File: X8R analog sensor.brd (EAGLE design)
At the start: 21.6 x 15.5 mm, 14 parts, among them IC1 MCP1703CB, U1 ATTINY13SOIC

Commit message: updated bypass caps as tantalums aren't needed
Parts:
- C2, C3: value 10uf 6.3V -> 1uf; device MyLib:CAP-0603 -> SparkFun-Capacitors:0603-CAP
- moved C2 4.49 mm to (5.08, 12.7), turned to 270 degrees
- moved C3 4.49 mm to (5.71, 8.26), turned to 180 degrees
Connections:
- net VCC: now also C3.1; no longer C2.1
- net VIN: now also C2.1; no longer C3.1
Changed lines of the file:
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@@
 </element>
 <element name="LED" library="SparkFun-LED" package="LED-0603" value="BLUE" x="6.985" y="12.7" smashed="yes">
-<attribute name="NAME" x="6.2865" y="11.176" size="0.4064" layer="25" rot="R90"/>
+<attribute name="NAME" x="6.4135" y="14.0335" size="0.4064" layer="25"/>
 <attribute name="VALUE" x="8.0645" y="11.684" size="0.4064" layer="27" rot="R90"/>
 </element>
@@
 <attribute name="NAME" x="7.5565" y="11.303" size="0.4064" layer="25" font="vector" rot="R180"/>
 <attribute name="VALUE" x="6.731" y="11.303" size="0.4064" layer="27" font="vector" rot="R180"/>
-</element>
-<element name="C2" library="MyLib" package="CAP-0603" value="10uf 6.3V" x="5.715" y="8.255" smashed="yes" rot="R180">
-<attribute name="NAME" x="7.239" y="9.398" size="0.4064" layer="25" font="vector" rot="R180"/>
-<attribute name="VALUE" x="6.731" y="9.398" size="0.4064" layer="27" font="vector" rot="R180"/>
-</element>
-<element name="C3" library="MyLib" package="CAP-0603" value="10uf 6.3V" x="5.08" y="12.7" smashed="yes" rot="R270">
-<attribute name="NAME" x="3.921" y="13.0175" size="0.4064" layer="25" rot="R270"/>
-<attribute name="VALUE" x="6.412" y="12.292" size="0.4064" layer="27" rot="R270"/>
 </element>
 <element name="FRAME1" library="SparkFun-Aesthetics" package="CREATIVE_COMMONS" value="FRAME-LETTER" x="-3.175" y="-11.43"/>
@@
 <attribute name="VALUE" x="19.5739" y="4.9155" size="0.8128" layer="21" ratio="15" rot="R270"/>
 </element>
+<element name="C2" library="SparkFun-Capacitors" package="0603-CAP" value="1uf" x="5.08" y="12.7" rot="R270"/>
+<element name="C3" library="SparkFun-Capacitors" package="0603-CAP" value="1uf" x="5.715" y="8.255" rot="R180"/>
 </elements>
 <signals>
 <signal name="GND">
-<contactref element="IC1" pad="1"/>
-<contactref element="C2" pad="2"/>
-<contactref element="C3" pad="2"/>
-<contactref element="C1" pad="2"/>
 <polygon width="0.4064" layer="1">
 <vertex x="0" y="15.5575"/>
@@
 <via x="19.05" y="3.4925" extent="1-16" drill="0.6"/>
 <via x="1.5875" y="1.5875" extent="1-16" drill="0.6"/>
+<contactref element="IC1" pad="1"/>
+<contactref element="C2" pad="2"/>
+<contactref element="C3" pad="2"/>
+<contactref element="C1" pad="2"/>
 </signal>
 <signal name="AIN">
@@
 <contactref element="IC1" pad="2"/>
 <contactref element="C1" pad="1"/>
-<contactref element="C2" pad="1"/>
-<wire x1="6.565" y1="8.255" x2="8.675" y2="8.255" width="0.4064" layer="1"/>
 <wire x1="10.475" y1="10.33" x2="10.475" y2="10.055" width="0.4064" layer="1"/>
 <wire x1="10.475" y1="10.055" x2="8.675" y2="8.255" width="0.4064" layer="1"/>
@@
 <wire x1="4.865" y1="9.74" x2="5.3975" y2="9.2075" width="0.4064" layer="1"/>
 <wire x1="5.3975" y1="9.2075" x2="5.6125" y2="9.2075" width="0.4064" layer="1"/>
-<wire x1="5.6125" y1="9.2075" x2="6.565" y2="8.255" width="0.4064" layer="1"/>
 <wire x1="4.1275" y1="4.445" x2="4.1275" y2="5.715" width="0.4064" layer="1"/>
 <wire x1="4.1275" y1="5.715" x2="5.08" y2="6.6675" width="0.4064" layer="1"/>
 <wire x1="5.08" y1="6.6675" x2="5.715" y2="6.6675" width="0.4064" layer="1"/>
 <wire x1="5.715" y1="6.6675" x2="6.565" y2="7.5175" width="0.4064" layer="1"/>
-<wire x1="6.565" y1="7.5175" x2="6.565" y2="8.255" width="0.4064" layer="1"/>
+<contactref element="C3" pad="1"/>
+<wire x1="5.6125" y1="9.2075" x2="6.565" y2="8.255" width="0.4064" layer="1"/>
+<wire x1="6.565" y1="8.255" x2="6.565" y2="7.5175" width="0.4064" layer="1"/>
+<wire x1="6.565" y1="8.255" x2="6.35" y2="8.255" width="0.4064" layer="1"/>
+<wire x1="6.565" y1="8.255" x2="8.675" y2="8.255" width="0.4064" layer="1"/>
 </signal>
 <signal name="N$7">
@@
 <contactref element="S-PORT" pad="2"/>
 <contactref element="IC1" pad="3"/>
-<contactref element="C3" pad="1"/>
-<wire x1="2.6425" y1="11.1125" x2="5.08" y2="13.55" width="0.4064" layer="1"/>
 <wire x1="9.525" y1="12.53" x2="9.525" y2="14.2875" width="0.4064" layer="1"/>
 <wire x1="9.525" y1="14.2875" x2="9.2075" y2="14.605" width="0.4064" layer="1"/>
 <wire x1="9.2075" y1="14.605" x2="6.135" y2="14.605" width="0.4064" layer="1"/>
+<wire x1="2.6425" y1="11.1125" x2="1.905" y2="11.1125" width="0.4064" layer="1"/>
+<contactref element="C2" pad="1"/>
 <wire x1="6.135" y1="14.605" x2="5.08" y2="13.55" width="0.4064" layer="1"/>
-<wire x1="2.6425" y1="11.1125" x2="1.905" y2="11.1125" width="0.4064" layer="1"/>
+<wire x1="5.08" y1="13.55" x2="2.6425" y2="11.1125" width="0.4064" layer="1"/>
 </signal>
 <signal name="AIN-O">

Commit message: updated for a bypass cap on the AIN side, and changed the 3 pin connector for AIN to a 2 pin
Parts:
- removed ANALOGIN: (no value), SparkFun-Connectors:1X03
- added ANALOG-IN: M02PTH, SparkFun-Connectors:1X02
- added C4: .1uf, SparkFun-Capacitors:0603-CAP
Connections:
- net AIN: now also ANALOG-IN.1; no longer ANALOGIN.1
- net AIN-O: now also C4.1
- net GND: now also ANALOG-IN.2, C4.2; no longer ANALOGIN.3
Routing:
- net AIN: track 3.24 -> 5.78 mm
- net AIN-O: track 19.9 -> 18.7 mm
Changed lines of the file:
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@@
 </autorouter>
 <elements>
-<element name="C1" library="SparkFun-Capacitors" package="0603-CAP" value=".1uf" x="9.525" y="8.255" smashed="yes">
-<attribute name="NAME" x="11.049" y="9.398" size="0.4064" layer="25" font="vector" rot="R180"/>
-<attribute name="VALUE" x="8.509" y="7.112" size="0.4064" layer="27" font="vector"/>
-</element>
-<element name="U1" library="SparkFun-DigitalIC" package="SO08" value="ATTINY13SOIC" x="14.605" y="7.9375" smashed="yes" rot="R180">
-<attribute name="VALUE" x="15.875" y="8.5725" size="0.4064" layer="27" rot="R180"/>
-<attribute name="NAME" x="11.43" y="6.985" size="0.4064" layer="25"/>
-</element>
+<element name="C1" library="SparkFun-Capacitors" package="0603-CAP" value=".1uf" x="9.525" y="8.255"/>
+<element name="U1" library="SparkFun-DigitalIC" package="SO08" value="ATTINY13SOIC" x="14.605" y="7.9375" rot="R180"/>
 <element name="IC1" library="linear" package="SOT23" value="MCP1703CB" x="9.525" y="11.43" smashed="yes">
 <attribute name="NAME" x="7.9375" y="12.3825" size="0.4064" layer="25"/>
@@
 <attribute name="NAME" x="2.9337" y="6.9088" size="0.4064" layer="25" ratio="10" rot="R180"/>
 <attribute name="VALUE" x="5.08" y="7.3025" size="1.27" layer="27" rot="R90"/>
-</element>
-<element name="ANALOGIN" library="SparkFun-Connectors" package="1X03" value="" x="19.685" y="8.5725" smashed="yes" rot="R90">
-<attribute name="NAME" x="18.1737" y="7.3787" size="0.4064" layer="25" ratio="10" rot="R90"/>
-<attribute name="VALUE" x="22.86" y="7.3025" size="1.27" layer="27" rot="R90"/>
 </element>
 <element name="LED" library="SparkFun-LED" package="LED-0603" value="BLUE" x="6.985" y="12.7" smashed="yes">
@@
 <element name="C2" library="SparkFun-Capacitors" package="0603-CAP" value="1uf" x="5.08" y="12.7" rot="R270"/>
 <element name="C3" library="SparkFun-Capacitors" package="0603-CAP" value="1uf" x="5.715" y="8.255" rot="R180"/>
+<element name="C4" library="SparkFun-Capacitors" package="0603-CAP" value=".1uf" x="15.5575" y="1.905" rot="R180"/>
+<element name="ANALOG-IN" library="SparkFun-Connectors" package="1X02" value="M02PTH" x="19.685" y="11.1125" smashed="yes" rot="R90">
+<attribute name="NAME" x="18.0213" y="9.1313" size="0.4064" layer="25" ratio="10"/>
+<attribute name="VALUE" x="22.86" y="9.8425" size="1.27" layer="27" rot="R90"/>
+</element>
 </elements>
 <signals>
@@
 </polygon>
 <contactref element="S-PORT" pad="1"/>
-<contactref element="ANALOGIN" pad="3"/>
 <contactref element="LED" pad="C"/>
 <contactref element="U1" pad="4"/>
@@
 <contactref element="R3" pad="1"/>
 <via x="10.795" y="13.97" extent="1-16" drill="0.6"/>
-<via x="13.97" y="2.2225" extent="1-16" drill="0.6"/>
+<via x="12.7" y="1.905" extent="1-16" drill="0.6"/>
 <via x="11.43" y="4.7625" extent="1-16" drill="0.6"/>
 <via x="19.05" y="3.4925" extent="1-16" drill="0.6"/>
@@
 <contactref element="C3" pad="2"/>
 <contactref element="C1" pad="2"/>
+<contactref element="C4" pad="2"/>
+<contactref element="ANALOG-IN" pad="2"/>
+<via x="19.685" y="7.9375" extent="1-16" drill="0.6"/>
 </signal>
 <signal name="AIN">
-<contactref element="ANALOGIN" pad="1"/>
 <contactref element="R2" pad="2"/>
-<wire x1="19.685" y1="8.5725" x2="18.0975" y2="6.985" width="0.4064" layer="1"/>
-<wire x1="18.0975" y1="6.985" x2="18.0975" y2="5.9925" width="0.4064" layer="1"/>
+<contactref element="ANALOG-IN" pad="1"/>
+<wire x1="19.685" y1="11.1125" x2="18.0975" y2="9.525" width="0.4064" layer="1"/>
+<wire x1="18.0975" y1="9.525" x2="18.0975" y2="5.9925" width="0.4064" layer="1"/>
 </signal>
 <signal name="VCC">
@@
 <contactref element="S-PORT" pad="2"/>
 <contactref element="IC1" pad="3"/>
-<wire x1="9.525" y1="12.53" x2="9.525" y2="14.2875" width="0.4064" layer="1"/>
-<wire x1="9.525" y1="14.2875" x2="9.2075" y2="14.605" width="0.4064" layer="1"/>
-<wire x1="9.2075" y1="14.605" x2="6.135" y2="14.605" width="0.4064" layer="1"/>
 <wire x1="2.6425" y1="11.1125" x2="1.905" y2="11.1125" width="0.4064" layer="1"/>
 <contactref element="C2" pad="1"/>
 <wire x1="6.135" y1="14.605" x2="5.08" y2="13.55" width="0.4064" layer="1"/>
 <wire x1="5.08" y1="13.55" x2="2.6425" y2="11.1125" width="0.4064" layer="1"/>
+<wire x1="9.525" y1="12.53" x2="9.525" y2="13.97" width="0.4064" layer="1"/>
+<wire x1="9.525" y1="13.97" x2="8.89" y2="14.605" width="0.4064" layer="1"/>
+<wire x1="8.89" y1="14.605" x2="6.135" y2="14.605" width="0.4064" layer="1"/>
 </signal>
 <signal name="AIN-O">
@@
 <contactref element="R3" pad="2"/>
 <contactref element="R2" pad="1"/>
+<contactref element="C4" pad="1"/>
+<wire x1="6.6675" y1="1.905" x2="7.9375" y2="0.635" width="0.4064" layer="1"/>
+<wire x1="7.9375" y1="0.635" x2="15.24" y2="0.635" width="0.4064" layer="1"/>
 <wire x1="20.0025" y1="0.9925" x2="18.0975" y2="0.9925" width="0.4064" layer="1"/>
-<wire x1="18.0975" y1="0.9925" x2="17.4225" y2="0.9925" width="0.4064" layer="1"/>
-<wire x1="17.4225" y1="0.9925" x2="15.24" y2="3.175" width="0.4064" layer="1"/>
-<wire x1="15.24" y1="3.175" x2="15.24" y2="5.3213" width="0.4064" layer="1"/>
-<wire x1="6.6675" y1="1.905" x2="7.9375" y2="0.635" width="0.4064" layer="1"/>
-<wire x1="7.9375" y1="0.635" x2="17.74" y2="0.635" width="0.4064" layer="1"/>
-<wire x1="17.74" y1="0.635" x2="18.0975" y2="0.9925" width="0.4064" layer="1"/>
+<wire x1="18.0975" y1="0.9925" x2="17.185" y2="1.905" width="0.4064" layer="1"/>
+<wire x1="17.185" y1="1.905" x2="16.4075" y2="1.905" width="0.4064" layer="1"/>
+<wire x1="16.4075" y1="1.905" x2="15.24" y2="3.0725" width="0.4064" layer="1"/>
+<wire x1="15.24" y1="3.0725" x2="15.24" y2="5.3213" width="0.4064" layer="1"/>
+<wire x1="16.4075" y1="1.905" x2="16.4075" y2="1.8025" width="0.4064" layer="1"/>
+<wire x1="16.4075" y1="1.8025" x2="15.24" y2="0.635" width="0.4064" layer="1"/>
 </signal>
 </signals>

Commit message: reverted back to the 3 pin connector on AIN
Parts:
- ANALOG-IN: value M02PTH -> (none); device SparkFun-Connectors:1X02 -> SparkFun-Connectors:1X03
- moved ANALOG-IN 2.54 mm to (19.7, 8.57)
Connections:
- net GND: now also ANALOG-IN.3; no longer ANALOG-IN.2
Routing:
- net AIN: track 5.78 -> 3.24 mm
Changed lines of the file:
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@@
 <element name="C3" library="SparkFun-Capacitors" package="0603-CAP" value="1uf" x="5.715" y="8.255" rot="R180"/>
 <element name="C4" library="SparkFun-Capacitors" package="0603-CAP" value=".1uf" x="15.5575" y="1.905" rot="R180"/>
-<element name="ANALOG-IN" library="SparkFun-Connectors" package="1X02" value="M02PTH" x="19.685" y="11.1125" smashed="yes" rot="R90">
-<attribute name="NAME" x="18.0213" y="9.1313" size="0.4064" layer="25" ratio="10"/>
-<attribute name="VALUE" x="22.86" y="9.8425" size="1.27" layer="27" rot="R90"/>
+<element name="ANALOG-IN" library="SparkFun-Connectors" package="1X03" value="" x="19.685" y="8.5725" smashed="yes" rot="R90">
+<attribute name="NAME" x="18.1737" y="7.2263" size="0.4064" layer="25" ratio="10" rot="R90"/>
+<attribute name="VALUE" x="22.86" y="7.3025" size="1.27" layer="27" rot="R90"/>
 </element>
 </elements>
@@
 <contactref element="C1" pad="2"/>
 <contactref element="C4" pad="2"/>
-<contactref element="ANALOG-IN" pad="2"/>
-<via x="19.685" y="7.9375" extent="1-16" drill="0.6"/>
+<contactref element="ANALOG-IN" pad="3"/>
 </signal>
 <signal name="AIN">
 <contactref element="R2" pad="2"/>
 <contactref element="ANALOG-IN" pad="1"/>
-<wire x1="19.685" y1="11.1125" x2="18.0975" y2="9.525" width="0.4064" layer="1"/>
-<wire x1="18.0975" y1="9.525" x2="18.0975" y2="5.9925" width="0.4064" layer="1"/>
+<wire x1="18.0975" y1="5.9925" x2="18.0975" y2="6.985" width="0.4064" layer="1"/>
+<wire x1="18.0975" y1="6.985" x2="19.685" y2="8.5725" width="0.4064" layer="1"/>
 </signal>
 <signal name="VCC">

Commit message: small non-functional tweaks to the board layout, updated gerbers
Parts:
- moved C4 1.00 mm to (16.5, 2.22), turned to 90 degrees
- moved R2 0.32 mm to (18.4, 3.49)
- moved R3 0.32 mm to (20.3, 3.49)
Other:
- board text added: "20131024-1"
- board text removed: "20131022-1"
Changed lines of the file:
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@@
 <text x="3.4925" y="8.255" size="0.8128" layer="21">-</text>
 <text x="17.78" y="8.255" size="0.8128" layer="22" font="vector" rot="MR0">X8R S.port-2-analog</text>
-<text x="17.78" y="6.985" size="0.6096" layer="22" font="vector" rot="MR0">20131022-1</text>
+<text x="17.78" y="6.985" size="0.6096" layer="22" font="vector" rot="MR0">20131024-1</text>
 <dimension x1="0" y1="0" x2="0" y2="15.5575" x3="-2.54" y3="7.77875" textsize="1.778" layer="49"/>
 <dimension x1="0" y1="15.5575" x2="21.59" y2="15.5575" x3="10.795" y3="17.78" textsize="1.778" layer="49"/>
@@
 <attribute name="VALUE" x="11.43" y="10.4775" size="1.27" layer="27"/>
 </element>
-<element name="R2" library="SparkFun-Passives" package="1/6W-RES" value="" x="18.0975" y="3.4925" smashed="yes" rot="R90">
-<attribute name="NAME" x="17.4652" y="4.7587" size="0.6096" layer="25" rot="R270"/>
-<attribute name="VALUE" x="18.5261" y="2.0695" size="0.8128" layer="21" ratio="15" rot="R90"/>
-</element>
-<element name="R3" library="SparkFun-Passives" package="1/6W-RES" value="" x="20.0025" y="3.4925" smashed="yes" rot="R270">
-<attribute name="NAME" x="19.3702" y="4.7587" size="0.6096" layer="25" rot="R270"/>
-<attribute name="VALUE" x="19.5739" y="4.9155" size="0.8128" layer="21" ratio="15" rot="R270"/>
+<element name="R2" library="SparkFun-Passives" package="1/6W-RES" value="" x="18.415" y="3.4925" smashed="yes" rot="R90">
+<attribute name="NAME" x="17.7827" y="4.7587" size="0.6096" layer="25" rot="R270"/>
+<attribute name="VALUE" x="18.8436" y="2.0695" size="0.8128" layer="21" ratio="15" rot="R90"/>
+</element>
+<element name="R3" library="SparkFun-Passives" package="1/6W-RES" value="" x="20.32" y="3.4925" smashed="yes" rot="R270">
+<attribute name="NAME" x="19.6877" y="4.7587" size="0.6096" layer="25" rot="R270"/>
+<attribute name="VALUE" x="19.8914" y="4.9155" size="0.8128" layer="21" ratio="15" rot="R270"/>
 </element>
 <element name="C2" library="SparkFun-Capacitors" package="0603-CAP" value="1uf" x="5.08" y="12.7" rot="R270"/>
 <element name="C3" library="SparkFun-Capacitors" package="0603-CAP" value="1uf" x="5.715" y="8.255" rot="R180"/>
-<element name="C4" library="SparkFun-Capacitors" package="0603-CAP" value=".1uf" x="15.5575" y="1.905" rot="R180"/>
+<element name="C4" library="SparkFun-Capacitors" package="0603-CAP" value=".1uf" x="16.51" y="2.2225" rot="R90"/>
 <element name="ANALOG-IN" library="SparkFun-Connectors" package="1X03" value="" x="19.685" y="8.5725" smashed="yes" rot="R90">
 <attribute name="NAME" x="18.1737" y="7.2263" size="0.4064" layer="25" ratio="10" rot="R90"/>
@@
 <signals>
 <signal name="GND">
-<polygon width="0.4064" layer="1">
+<polygon width="0.4064" layer="1" orphans="yes">
 <vertex x="0" y="15.5575"/>
 <vertex x="21.59" y="15.5575"/>
@@
 <vertex x="0" y="0"/>
 </polygon>
-<polygon width="0.4064" layer="16">
+<polygon width="0.4064" layer="16" orphans="yes">
 <vertex x="0" y="15.5575"/>
 <vertex x="21.59" y="15.5575"/>
@@
 <contactref element="U1" pad="4"/>
 <contactref element="ISP" pad="6"/>
-<via x="3.81" y="14.605" extent="1-16" drill="0.6"/>
 <contactref element="R3" pad="1"/>
-<via x="10.795" y="13.97" extent="1-16" drill="0.6"/>
-<via x="12.7" y="1.905" extent="1-16" drill="0.6"/>
-<via x="11.43" y="4.7625" extent="1-16" drill="0.6"/>
-<via x="19.05" y="3.4925" extent="1-16" drill="0.6"/>
-<via x="1.5875" y="1.5875" extent="1-16" drill="0.6"/>
+<via x="10.795" y="13.97" extent="1-16" drill="0.5"/>
+<via x="19.3675" y="3.4925" extent="1-16" drill="0.5"/>
+<via x="1.5875" y="1.5875" extent="1-16" drill="0.5"/>
 <contactref element="IC1" pad="1"/>
 <contactref element="C2" pad="2"/>
@@
 <contactref element="C4" pad="2"/>
 <contactref element="ANALOG-IN" pad="3"/>
+<via x="11.43" y="6.985" extent="1-16" drill="0.5"/>
 </signal>
 <signal name="AIN">
 <contactref element="R2" pad="2"/>
 <contactref element="ANALOG-IN" pad="1"/>
-<wire x1="18.0975" y1="5.9925" x2="18.0975" y2="6.985" width="0.4064" layer="1"/>
-<wire x1="18.0975" y1="6.985" x2="19.685" y2="8.5725" width="0.4064" layer="1"/>
+<wire x1="19.685" y1="8.5725" x2="18.415" y2="7.3025" width="0.4064" layer="1"/>
+<wire x1="18.415" y1="7.3025" x2="18.415" y2="5.9925" width="0.4064" layer="1"/>
 </signal>
 <signal name="VCC">
@@
 <contactref element="C4" pad="1"/>
 <wire x1="6.6675" y1="1.905" x2="7.9375" y2="0.635" width="0.4064" layer="1"/>
-<wire x1="7.9375" y1="0.635" x2="15.24" y2="0.635" width="0.4064" layer="1"/>
-<wire x1="20.0025" y1="0.9925" x2="18.0975" y2="0.9925" width="0.4064" layer="1"/>
-<wire x1="18.0975" y1="0.9925" x2="17.185" y2="1.905" width="0.4064" layer="1"/>
-<wire x1="17.185" y1="1.905" x2="16.4075" y2="1.905" width="0.4064" layer="1"/>
-<wire x1="16.4075" y1="1.905" x2="15.24" y2="3.0725" width="0.4064" layer="1"/>
-<wire x1="15.24" y1="3.0725" x2="15.24" y2="5.3213" width="0.4064" layer="1"/>
-<wire x1="16.4075" y1="1.905" x2="16.4075" y2="1.8025" width="0.4064" layer="1"/>
-<wire x1="16.4075" y1="1.8025" x2="15.24" y2="0.635" width="0.4064" layer="1"/>
+<wire x1="7.9375" y1="0.635" x2="15.7725" y2="0.635" width="0.4064" layer="1"/>
+<wire x1="20.32" y1="0.9925" x2="18.415" y2="0.9925" width="0.4064" layer="1"/>
+<wire x1="18.415" y1="0.9925" x2="16.89" y2="0.9925" width="0.4064" layer="1"/>
+<wire x1="16.89" y1="0.9925" x2="16.51" y2="1.3725" width="0.4064" layer="1"/>
+<wire x1="15.7725" y1="0.635" x2="16.51" y2="1.3725" width="0.4064" layer="1"/>
+<wire x1="16.51" y1="1.3725" x2="15.24" y2="2.6425" width="0.4064" layer="1"/>
+<wire x1="15.24" y1="2.6425" x2="15.24" y2="5.3213" width="0.4064" layer="1"/>
 </signal>
 </signals>

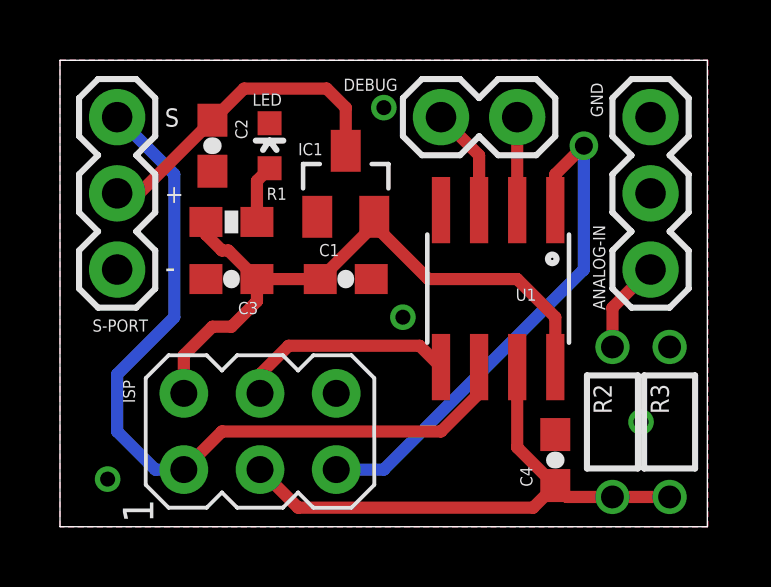
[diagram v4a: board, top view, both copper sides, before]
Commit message: updated v2 version with separate grounds
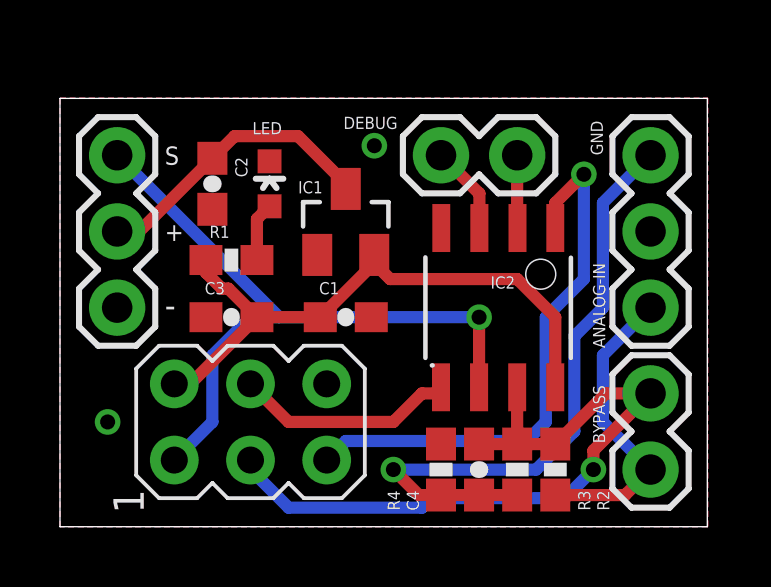
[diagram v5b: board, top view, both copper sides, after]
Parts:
- removed ISP: AVRISP-6, adafruit:AVRISP
- removed U1: ATTINY13SOIC, SparkFun-DigitalIC:SO08
- added BYPASS: M02PTH, SparkFun-Connectors:1X02
- added IC2: TINY13V-10SSU, atmel:8S1
- added ISP1: AVRISP-6, adafruit:AVRISP
- added R4: 1k0, SparkFun-Resistors:0603-RES
- R2: value (none) -> 15k; device SparkFun-Passives:1/6W-RES -> SparkFun-Passives:0603-RES
- R3: value (none) -> 3k3; device SparkFun-Passives:1/6W-RES -> SparkFun-Passives:0603-RES
- moved R3 5.32 mm to (15.2, 1.91), turned to 90 degrees
- moved C4 2.56 mm to (14.0, 1.91), turned to 270 degrees
- moved R2 2.48 mm to (16.5, 1.91), turned to 270 degrees
- moved C1 1.27 mm to (9.53, 6.99)
- moved C3 1.27 mm to (5.71, 6.99)
- moved ANALOG-IN 1.27 mm to (19.7, 7.30)
- moved C2 1.27 mm to (5.08, 11.4)
- moved DEBUG 1.27 mm to (12.7, 12.4)
- moved IC1 1.27 mm to (9.53, 10.2)
- moved LED 1.27 mm to (6.99, 11.4)
- moved R1 1.27 mm to (5.71, 8.89)
- moved S-PORT 1.27 mm to (1.91, 7.30)
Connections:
- removed net AIN-O: C4.1, ISP.3, R2.1, R3.2, U1.7
- removed net NRES: ISP.5, U1.1
- new net ADC1: BYPASS.2, C4.1, IC2.7, ISP1.3, R2.1, R3.2
- new net GND-A: ANALOG-IN.3, C4.2, R3.1, R4.2
- new net NRST: IC2.1, ISP1.5
- net ADC2: now also IC2.3; no longer U1.3
- net ADC3: now also IC2.2; no longer U1.2
- net AIN: now also BYPASS.1
- net GND: now also IC2.4, ISP1.6, R4.1; no longer ANALOG-IN.3, C4.2, ISP.6, R3.1, U1.4
- net MOSI: now also IC2.5, ISP1.4; no longer ISP.4, U1.5
- net SPORT: now also IC2.6, ISP1.1; no longer ISP.1, U1.6
- net VCC: now also IC2.8, ISP1.2; no longer ISP.2, U1.8
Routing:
- net ADC1: track 0.00 -> 24.4 mm, vias 0 -> 1
- net GND-A: track 0.00 -> 21.3 mm, vias 0 -> 1
- net AIN-O: track 19.1 -> 0.00 mm
- net NRST: track 0.00 -> 19.1 mm, vias 0 -> 1
- net NRES: track 17.7 -> 0.00 mm, vias 1 -> 0
- net AIN: track 3.11 -> 10.2 mm
- net SPORT: track 26.6 -> 23.4 mm, vias 0 -> 1
- net VCC: track 22.0 -> 20.5 mm
- net VIN: track 10.8 -> 9.76 mm
- net ADC2: track 3.62 -> 2.96 mm
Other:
- board size 21.6 x 15.5 mm -> 21.6 x 14.3 mm
- board text added: "20131105-1"
- board text removed: "20131024-1"
